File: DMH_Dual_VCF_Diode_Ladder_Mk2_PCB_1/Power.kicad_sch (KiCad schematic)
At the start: 32 parts, among them J0 Conn_01x01, J100 IDC_02x08, U1 TL074, U2 TL074, U3 TL074, U4 TL074, U5 TL074, U6 TL074, U7 TL074

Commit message: Added inter-board pins to all circuits
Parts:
- added J23: Conn_01x04_PinHeader, Connector_PinHeader_2.54mm:PinHeader_1x10_P2.54mm_Vertical, symbol SynthStuff:Conn_01x04_PinHeader
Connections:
- net +12V: now also J23.1 (Pin_1)
- net -12V: now also J23.2 (Pin_2)
- net GND: now also J23.3 (Pin_3), J23.4 (Pin_4)

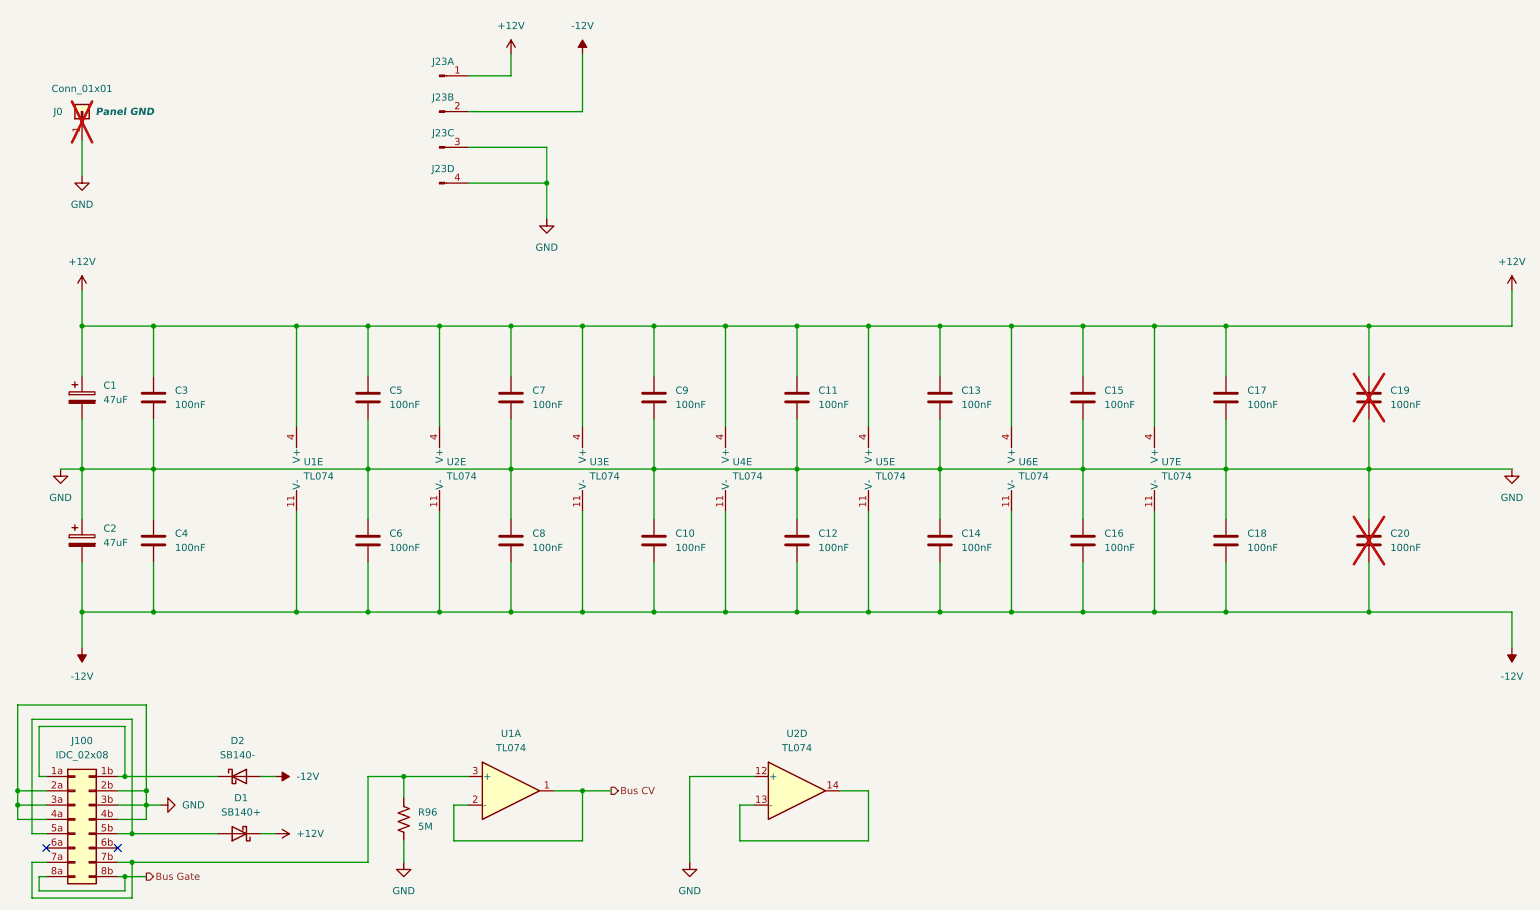
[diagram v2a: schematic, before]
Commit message: Reannotated OpAmps and cleared errors
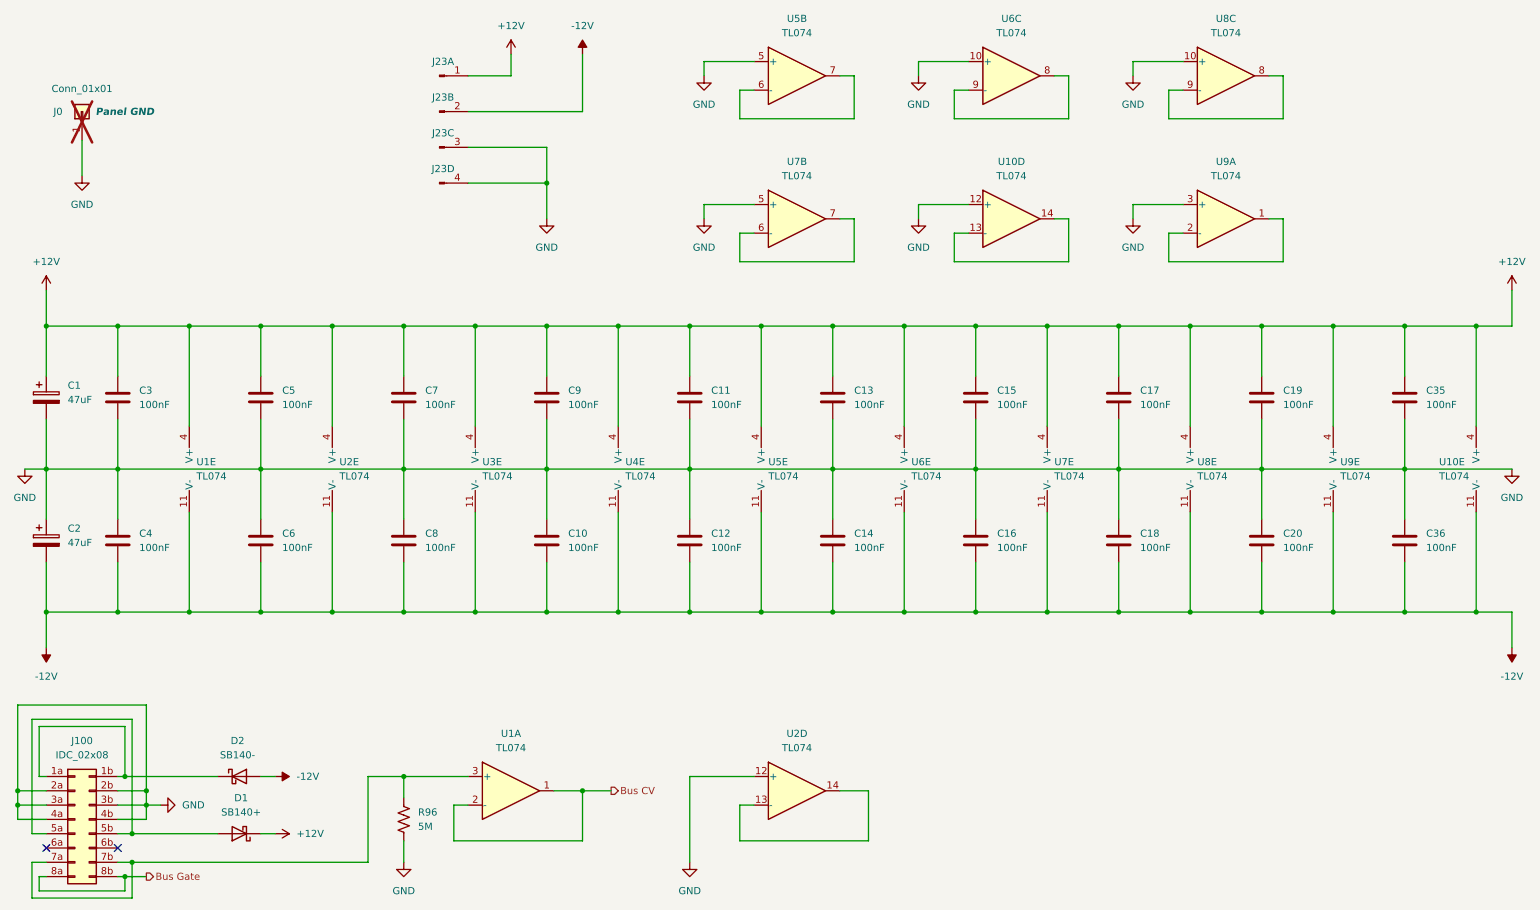
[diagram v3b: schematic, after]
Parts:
- added C35, C36: 100nF, Capacitor_THT:C_Disc_D4.3mm_W1.9mm_P5.00mm, symbol Device:C
- added U10, U8, U9: TL074, symbol Amplifier_Operational:TL074
- added unit 2 of U5
- added unit 3 of U6
- added unit 2 of U7
- C19, C20: now fitted; now in the parts list
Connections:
- net +12V: now also C35.1, U10.4 (V+), U8.4 (V+), U9.4 (V+)
- net -12V: now also C36.2, U10.11 (V-), U8.11 (V-), U9.11 (V-)
- net GND: now also C35.2, C36.1, U10.12 (+), U5.5 (+), U6.10 (+), U7.5 (+), U8.10 (+), U9.3 (+)
- new net: U5.6 (-), U5.7
- new net: U10.13 (-), U10.14
- new net: U6.8, U6.9 (-)
- new net: U7.6 (-), U7.7
- new net: U9.1, U9.2 (-)
- new net: U8.8, U8.9 (-)
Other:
- moved on the sheet: C1, C10, C11, C12, C13, C14, C15, C16, C17, C18, C2, C3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
